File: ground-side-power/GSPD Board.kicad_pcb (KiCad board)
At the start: 2 copper layers, 289.1 x 216.1 mm, 94 parts, among them J1 Battery Terminals, J10 Conn_01x03_Female, J12 Conn_01x04_Female, J13 DAQ Voltage Sensing, J14 DAQ Current Sensing, J15 To Router, J16 To RLCS, J17 To DAQ Laptop, J18 Conn_01x02_Female, J19 Conn_01x02_Female, J2 Battery Terminals, J20 To Ethernet, J21 To 5V M12, J22 To DAQ, J23 Extra M12, J24 Extra M12, J25 Extra M12, J26 Conn_01x02_Female, J27 Conn_01x02_Female, J3 Battery Terminals, J4 Battery Terminals, J5 874270842, J6 874270842, J7 ATX-24, J8 Conn_01x03_Female, J9 Conn_01x03_Female, K1 AZ2150-1A-12DEF, M1 Fan_PC_Chassis, M2 Fan_PC_Chassis, SW1 GRB234A2NABA1, U1 INA180, U2 INA180, U3 K7805-3AR3, U4 INA180, U5 INA180, U6 URB2424LD-20WR3

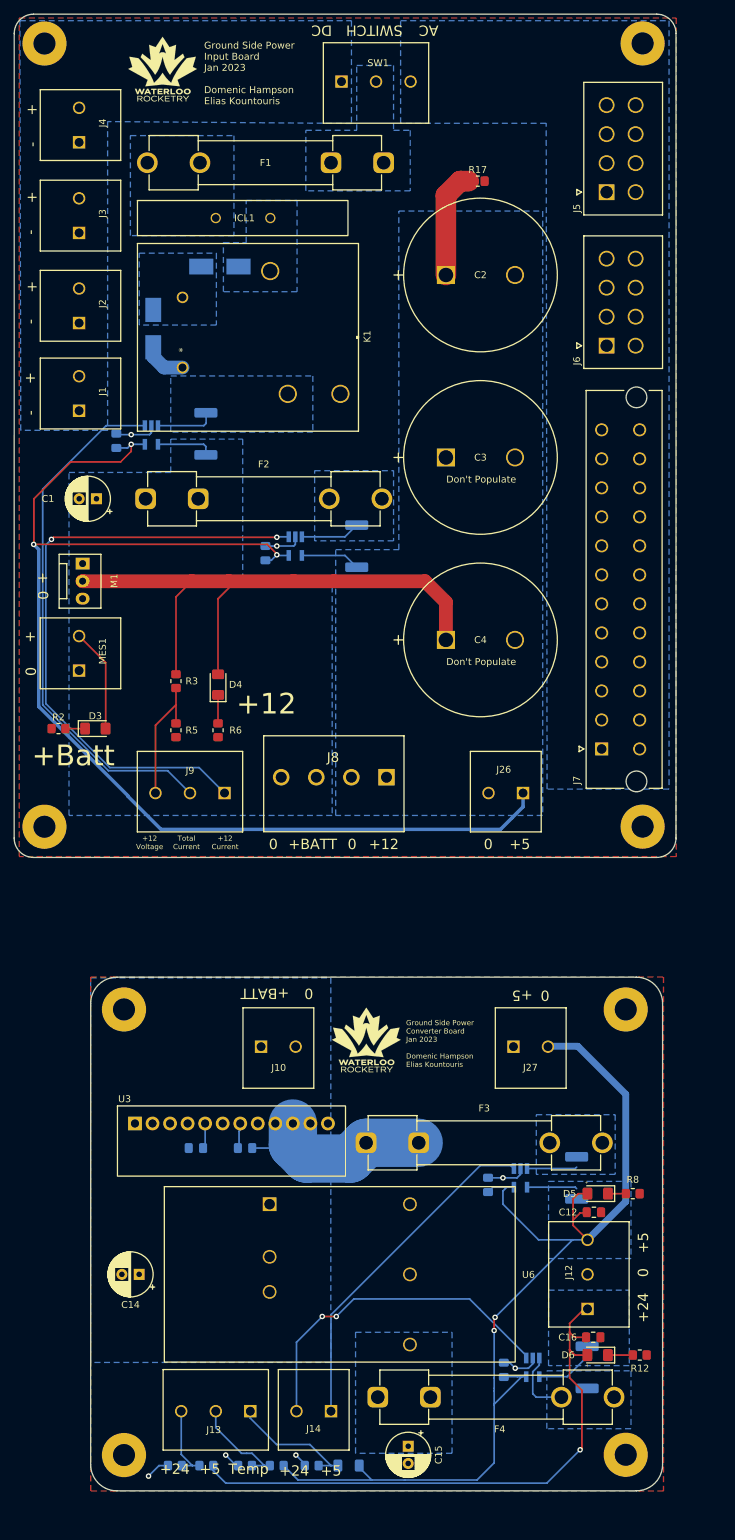
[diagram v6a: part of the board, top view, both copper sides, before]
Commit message: resolved issues from testing
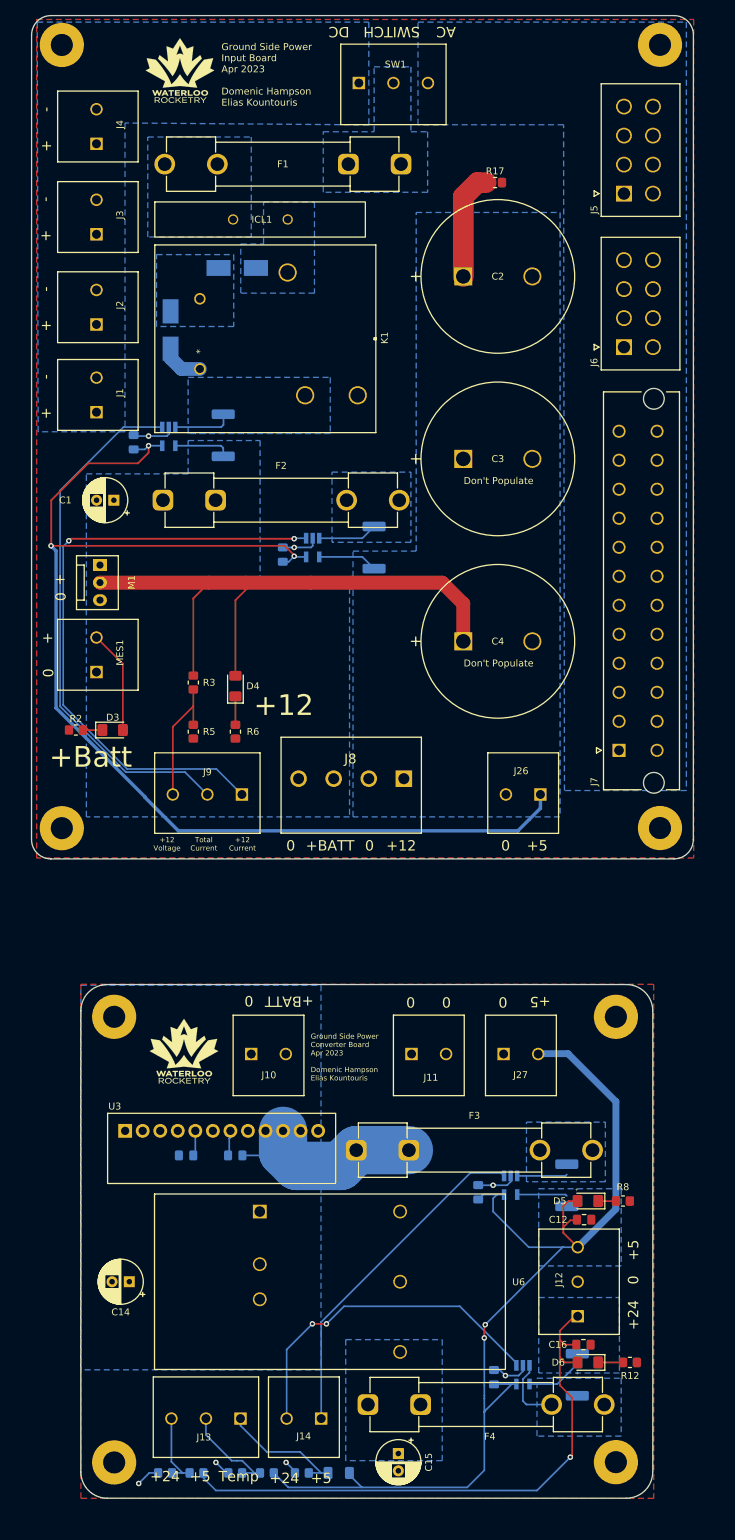
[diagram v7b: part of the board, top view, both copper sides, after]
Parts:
- removed the ? at (30.0, -105.9)
- removed the ? at (30.0, -41.4)
- removed the ? at (18.5, -128.2)
- removed the ? at (102.6, -105.9)
- removed the ? at (105.1, -241.6)
- removed the ? at (105.1, -128.2)
- removed the ? at (102.6, -41.5)
- removed the G*** at (35.6, -237.9)
- removed the G*** at (65.1, -97.3)
- added ?: , clipboard:6b5716c7-8553-4764-af17-05841c85de2e, F.Cu at (101.2, -40.4)
- added ?: , clipboard:6b5716c7-8553-4764-af17-05841c85de2e, F.Cu at (28.5, -104.9)
- added ?: , , F.Cu at (107.6, -128.0)
- added ?: , clipboard:6b5716c7-8553-4764-af17-05841c85de2e, F.Cu at (101.2, -104.9)
- added ?: , , F.Cu at (107.6, -241.4)
- added ?: , clipboard:6b5716c7-8553-4764-af17-05841c85de2e, F.Cu at (28.5, -40.3)
- added ?: , , F.Cu at (21.0, -128.0)
- added G***: LOGO, rlcs:rocketry_logo_small, F.Cu at (38.7, -95.7)
- added G***: LOGO, rlcs:rocketry_logo_small, F.Cu at (38.1, -237.7)
- added J11: Ground Connections, GSP:1935310, F.Cu at (71.6, -95.3)
- moved C4 2.52 mm to (79.1, -155.0)
- moved J6 2.52 mm to (102.4, -197.6)
- moved K1 2.52 mm to (41.0, -194.5)
- moved C1 2.52 mm to (28.5, -175.5)
- moved C2 2.52 mm to (79.1, -207.9)
- moved C3 2.52 mm to (79.1, -181.4)
- moved D4 2.52 mm to (46.1, -148.5)
- moved F1 2.52 mm to (70.1, -224.1)
- moved F2 2.52 mm to (35.6, -175.5)
- moved J1 2.52 mm to (26.0, -188.2)
- moved J2 2.52 mm to (26.0, -200.9)
- moved J3 2.52 mm to (26.0, -214.0)
- moved J4 2.52 mm to (26.0, -227.1)
- moved J5 2.52 mm to (102.4, -219.8)
- moved J7 2.52 mm to (101.6, -139.2)
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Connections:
- C10 pad 1: Net-(C10-Pad1) -> (no net)
- C15 pad 1: Net-(C15-Pad1) -> (no net)
- D5 pad 1: Net-(D5-Pad1) -> (no net)
- D6 pad 1: Net-(D6-Pad1) -> (no net)
- F3 pad 1: Net-(C10-Pad1) -> (no net)
- F4 pad 1: Net-(C15-Pad1) -> (no net)
- R12 pad 2: Net-(D6-Pad1) -> (no net)
- R8 pad 2: Net-(D5-Pad1) -> (no net)
- U3 pad 1: unconnected-(U3-Pad1) -> (no net)
- U3 pad 10: Net-(C10-Pad1) -> (no net)
- U3 pad 11: Net-(C10-Pad1) -> (no net)
- U3 pad 12: unconnected-(U3-Pad12) -> (no net)
- U3 pad 9: Net-(C10-Pad1) -> (no net)
- U6 pad 1: unconnected-(U6-Pad1) -> (no net)
- U6 pad 4: Net-(C15-Pad1) -> (no net)
- U6 pad 5: GND -> (no net)
- U6 pad 6: unconnected-(U6-Pad6) -> GND
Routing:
- net (no net): track 362.8 -> 398.3 mm
- net Net-(C10-Pad1): track 29.3 -> 0.00 mm
- net Net-(D6-Pad1): track 3.61 -> 0.00 mm
- net Net-(D5-Pad1): track 2.59 -> 0.00 mm
- removed copper zone on B.Cu, net Net-(C15-Pad1)
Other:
- board size 289.1 x 216.1 mm -> 286.6 x 215.9 mm
- board text added: "Ground Side Power Converter Board Apr 2023 Domenic Hampson Elias Kountouris"
- board text added: "Ground Side Power Input Board Apr 2023 Domenic Hampson Elias Kountouris"
- board text removed: "Ground Side Power Converter Board Jan 2023 Domenic Hampson Elias Kountouris"
- board text removed: "Ground Side Power Input Board Jan 2023 Domenic Hampson Elias Kountouris"
